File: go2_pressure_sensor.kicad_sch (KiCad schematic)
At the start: 11 parts, among them J1 Conn_01x03_Socket, U1 XPGZP6859A, U2 LP2980-ADJ

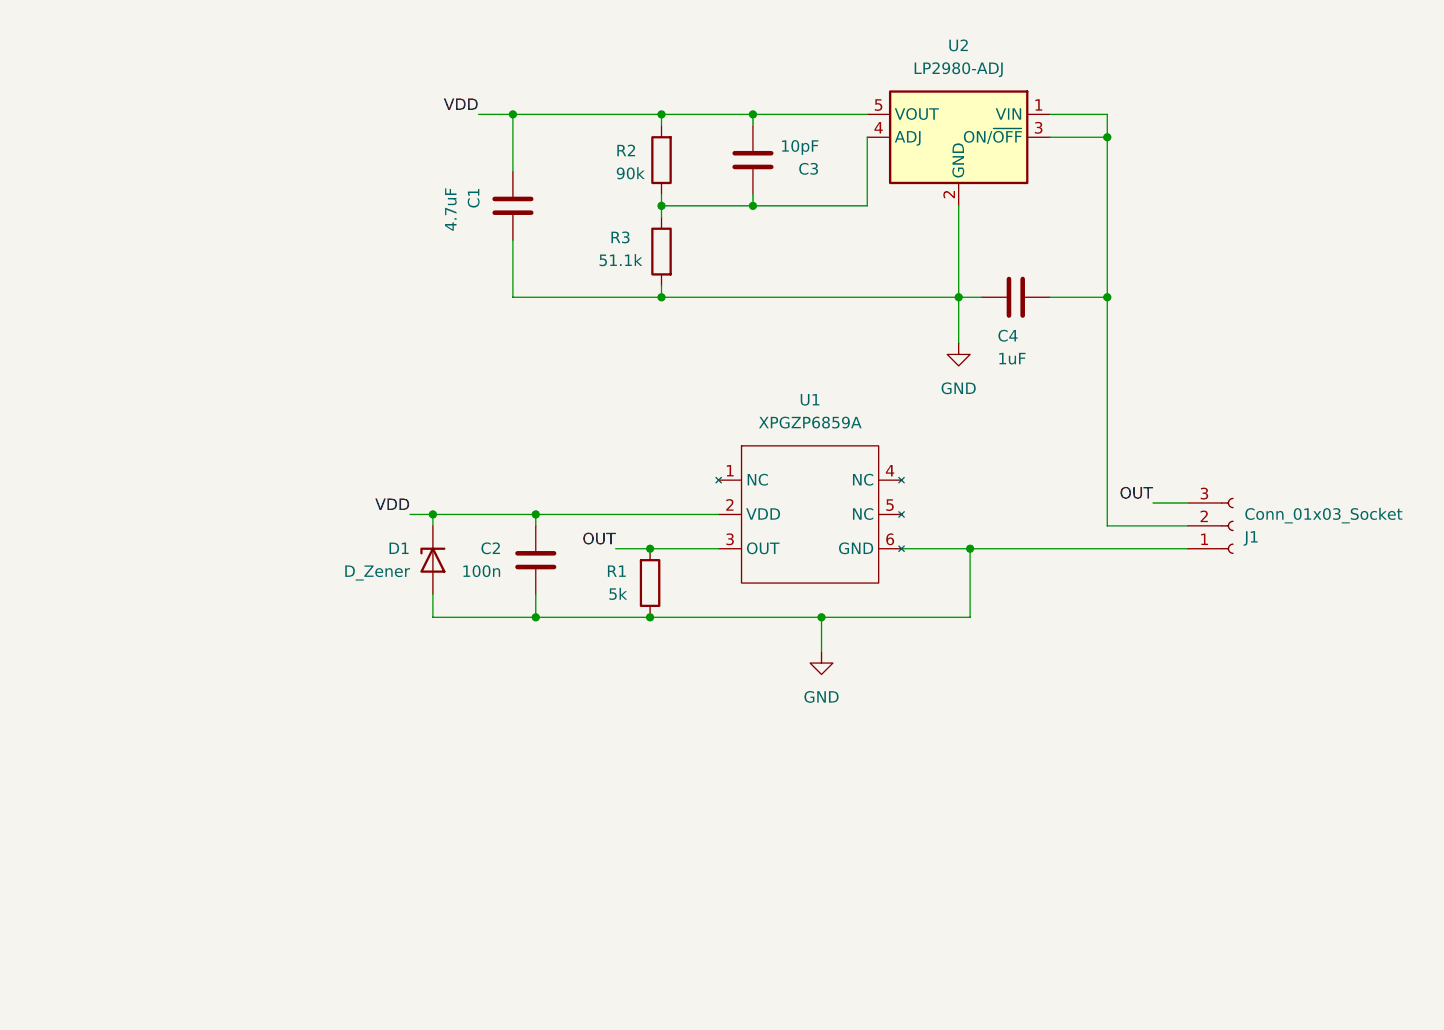
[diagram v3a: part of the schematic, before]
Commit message: Added silkscreen markings for pressure sensor
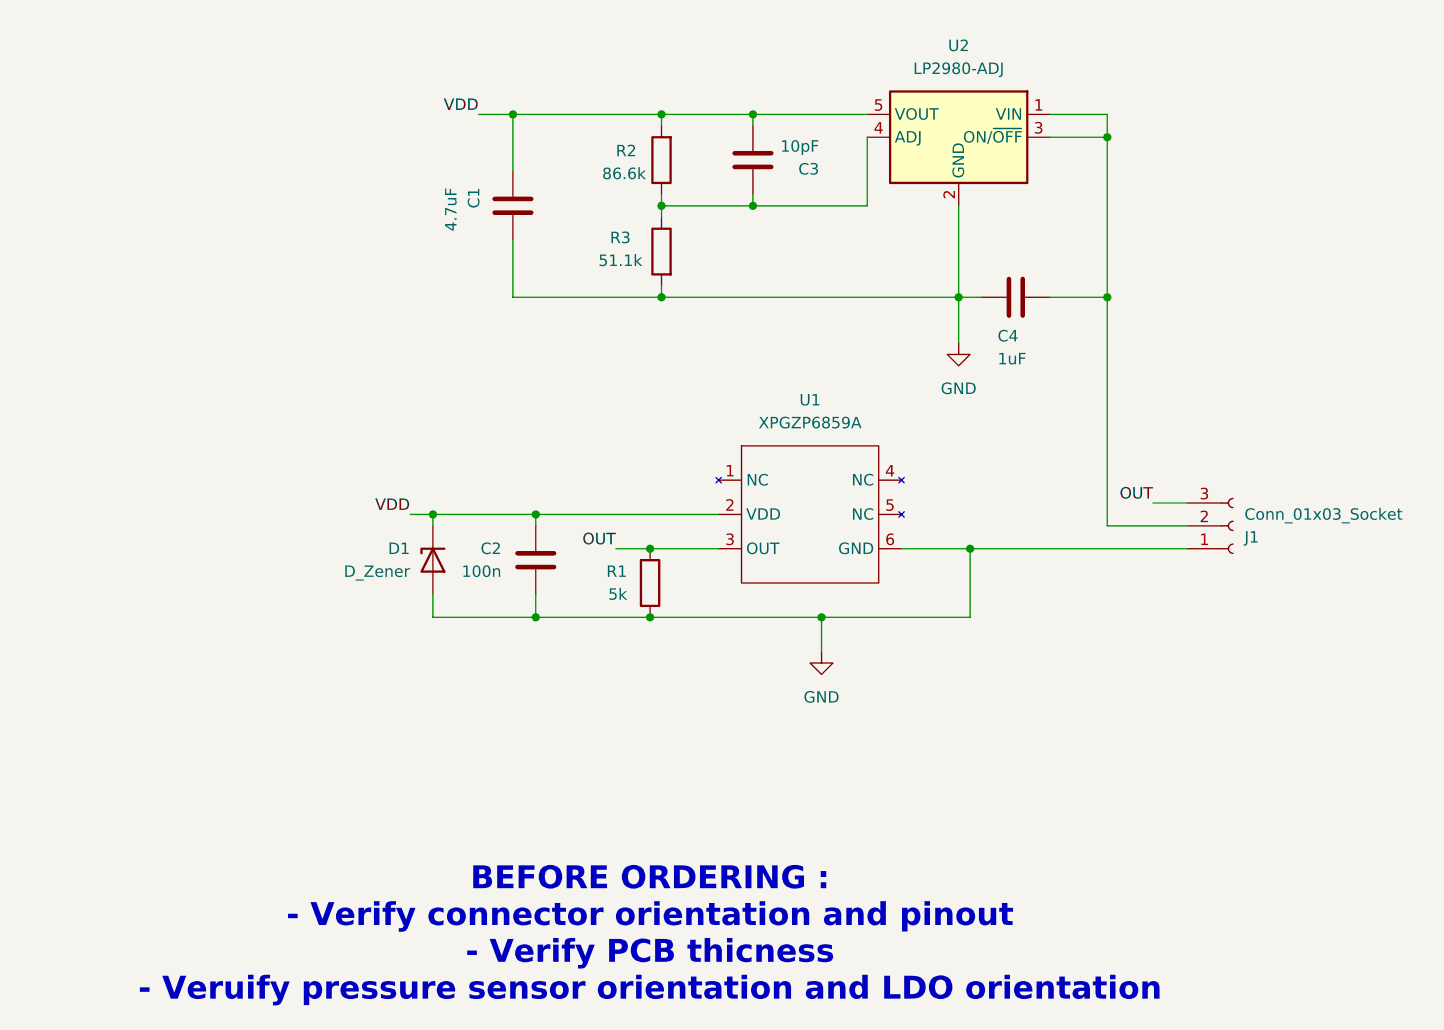
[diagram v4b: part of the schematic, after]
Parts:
- R2: value 90k -> 86.6k; LCSC C23129 -> C3000725
- U2: LCSC C5310801 -> C181526
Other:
- note added: "BEFORE ORDERING : - Verify connector orientation and pinout - Verify PCB thicness - Veruify pressure sensor orientation and LDO orientation"
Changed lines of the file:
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@@
+		)
+	)
+	(text "BEFORE ORDERING : \n- Verify connector orientation and pinout\n- Verify PCB thicness\n- Veruify pressure sensor orientation and LDO orientation"
+		(exclude_from_sim no)
+		(at 78.74 166.116 0)
+		(effects
+			(font
+				(size 2.54 2.54)
+				(thickness 0.508)
+				(bold yes)
+				(color 255 146 16 1)
+			)
 		)
 	)
@@
 			)
 		)
-		(property "LCSC" "C5310801"
+		(property "LCSC" "C181526"
 			(at 113.03 77.47 0)
 			(effects
@@
 			)
 		)
-		(property "Value" "90k"
-			(at 74.93 81.534 0)
+		(property "Value" "86.6k"
+			(at 73.406 81.534 0)
 			(effects
 				(font
@@
 			)
 		)
-		(property "LCSC" "C23129"
+		(property "LCSC" "C3000725"
 			(at 80.01 80.01 0)
 			(effects
